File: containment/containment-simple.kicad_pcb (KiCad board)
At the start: 2 copper layers, 45.7 x 45.7 mm, 36 parts, among them J1 Conn_02x05_Odd_Even, J3 Conn_01x02, J4 Conn_01x02, J5 Conn_01x02, J6 Conn_01x02, Q1 BSS84, Q2 BSS84, Q3 BSS84, Q4 BSS84, U1 TMP411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

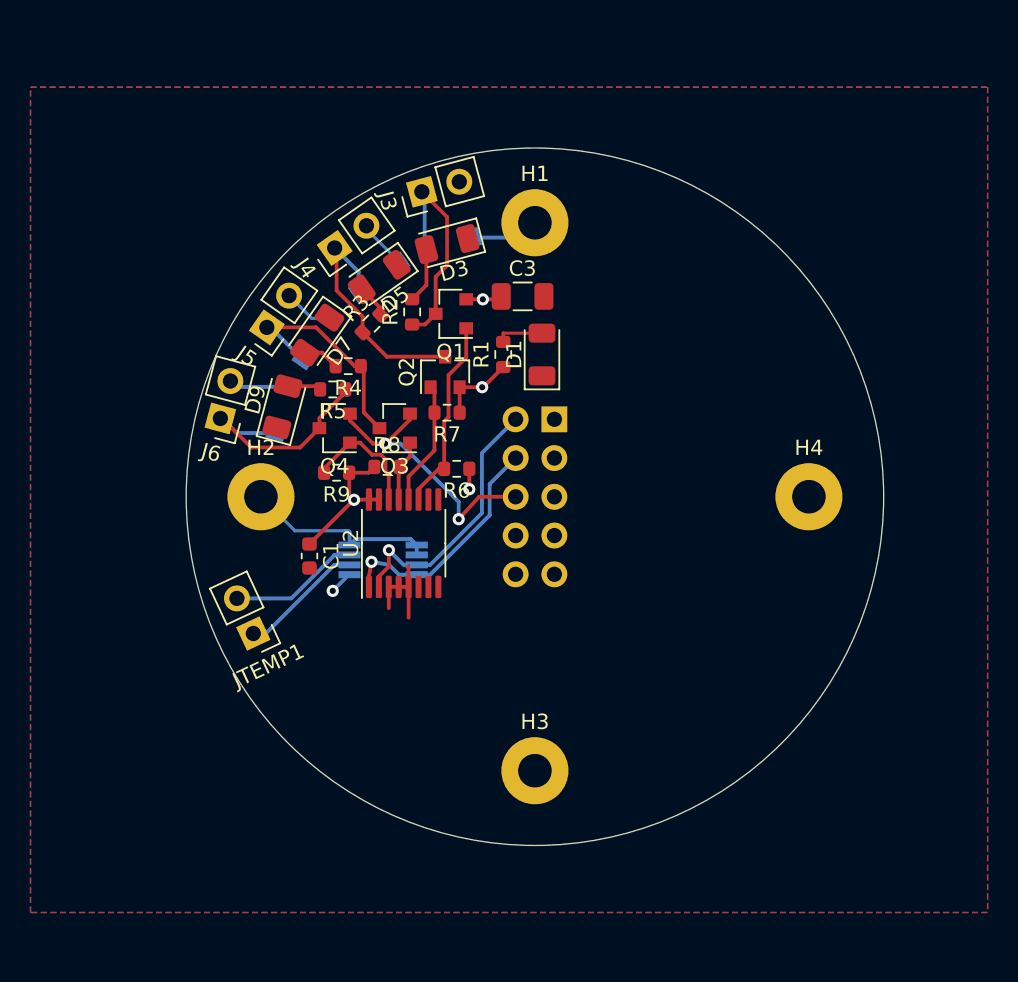
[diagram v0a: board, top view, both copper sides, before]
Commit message: add spixes
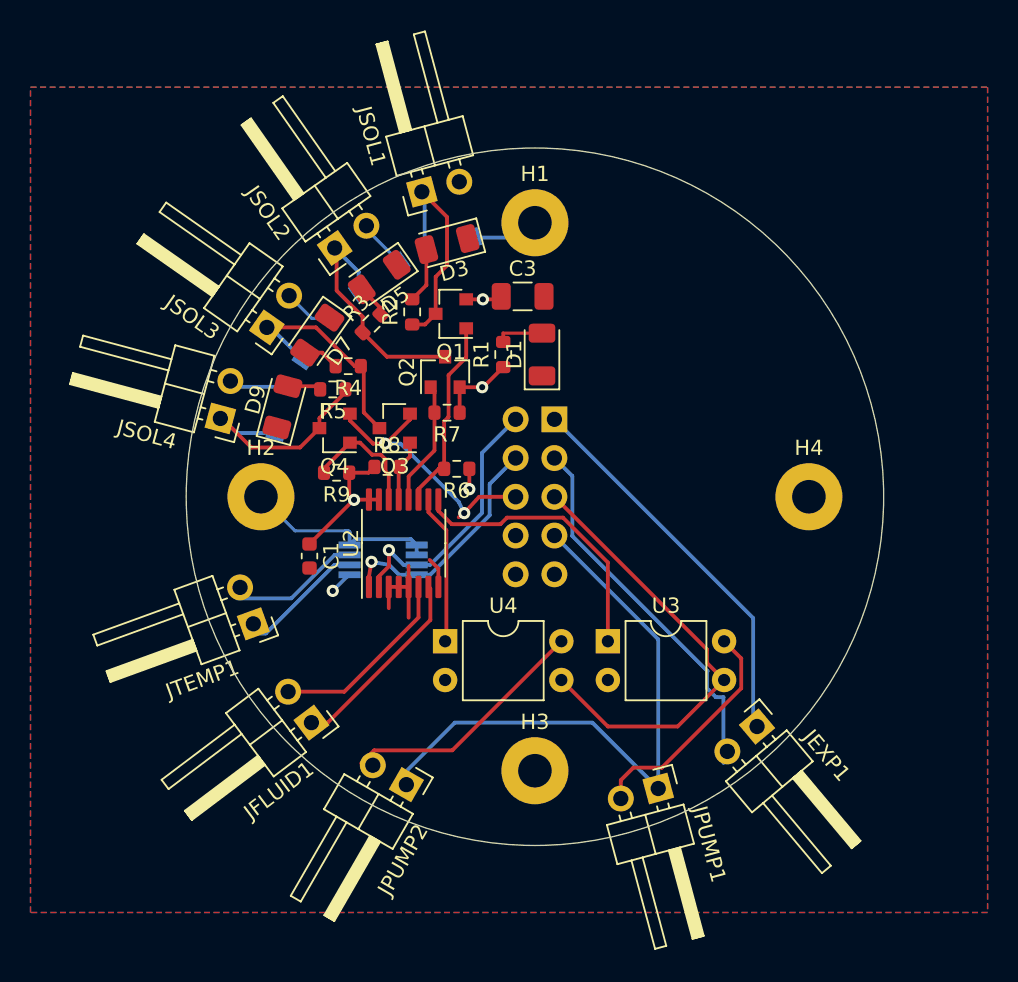
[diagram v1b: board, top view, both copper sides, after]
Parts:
- added JEXP1: Conn_01x02, Connector_PinHeader_2.54mm:PinHeader_1x02_P2.54mm_Horizontal, F.Cu at (154.6, 115.1)
- added JFLUID1: Conn_01x02, Connector_PinHeader_2.54mm:PinHeader_1x02_P2.54mm_Horizontal, F.Cu at (125.3, 114.8)
- added JPUMP1: Conn_01x02, Connector_PinHeader_2.54mm:PinHeader_1x02_P2.54mm_Horizontal, F.Cu at (148.1, 119.1)
- added JPUMP2: Conn_01x02, Connector_PinHeader_2.54mm:PinHeader_1x02_P2.54mm_Horizontal, F.Cu at (131.6, 118.9)
- added U3: SFH617A-1, Package_DIP:DIP-4_W7.62mm, F.Cu at (144.8, 109.5)
- added U4: SFH617A-1, Package_DIP:DIP-4_W7.62mm, F.Cu at (134.1, 109.5)
- JSOL1: renamed from J3; footprint Connector_PinHeader_2.54mm:PinHeader_1x02_P2.54mm_Vertical -> Connector_PinHeader_2.54mm:PinHeader_1x02_P2.54mm_Horizontal
- JSOL2: renamed from J4; footprint Connector_PinHeader_2.54mm:PinHeader_1x02_P2.54mm_Vertical -> Connector_PinHeader_2.54mm:PinHeader_1x02_P2.54mm_Horizontal
- JSOL3: renamed from J5; footprint Connector_PinHeader_2.54mm:PinHeader_1x02_P2.54mm_Vertical -> Connector_PinHeader_2.54mm:PinHeader_1x02_P2.54mm_Horizontal
- JSOL4: renamed from J6; footprint Connector_PinHeader_2.54mm:PinHeader_1x02_P2.54mm_Vertical -> Connector_PinHeader_2.54mm:PinHeader_1x02_P2.54mm_Horizontal
- JTEMP1: footprint Connector_PinHeader_2.54mm:PinHeader_1x02_P2.54mm_Vertical -> Connector_PinHeader_2.54mm:PinHeader_1x02_P2.54mm_Horizontal
- moved JTEMP1 0.63 mm to (121.5, 108.3), turned to 200 degrees
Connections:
- J1 pad 1: Net-(J1-Pad1) -> /experiment-
- J1 pad 3: Net-(J1-Pad3) -> /experiment+
- J1 pad 5: Net-(J1-Pad5) -> /HV-
- J1 pad 7: Net-(J1-Pad7) -> /HV+
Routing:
- net /HV+: track 0.00 -> 40.1 mm
- net /HV-: track 0.00 -> 29.8 mm
- net /experiment-: track 0.00 -> 26.3 mm
- net /experiment+: track 0.00 -> 24.9 mm
- net /p2: track 0.00 -> 18.8 mm
- net Net-(JPUMP2-Pad2): track 0.00 -> 16.4 mm
- net Net-(JPUMP1-Pad2): track 0.00 -> 15.1 mm
- net /p0: track 0.00 -> 12.9 mm
- net /p1: track 0.00 -> 12.8 mm
- net /p3: track 0.00 -> 9.81 mm
- net GND: track 33.5 -> 35.5 mm
- net +12V: track 18.1 -> 17.6 mm

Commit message: spikey 2
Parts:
- added JFLUID2: Conn_01x03, Connector_PinHeader_2.54mm:PinHeader_1x03_P2.54mm_Horizontal, F.Cu at (134.9, 120.3)
- JFLUID1: value Conn_01x02 -> Conn_01x03; footprint Connector_PinHeader_2.54mm:PinHeader_1x02_P2.54mm_Horizontal -> Connector_PinHeader_2.54mm:PinHeader_1x03_P2.54mm_Horizontal
- moved JPUMP2 16.4 mm to (148.0, 119.3), turned to 285 degrees
- moved JEXP1 7.51 mm to (158.4, 108.6), turned to 330 degrees
- moved JPUMP1 6.66 mm to (153.5, 115.3), turned to 310 degrees
- moved JFLUID1 1.71 mm to (126.6, 116.0), turned to 220 degrees
- moved U3 0.65 mm to (144.7, 108.8)
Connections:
- JFLUID1 pad 1: /p1 -> /p0
- JFLUID1 pad 2: /p0 -> +5V
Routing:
- net /HV+: track 40.1 -> 26.1 mm
- net Net-(JPUMP1-Pad2): track 15.1 -> 9.32 mm
- net /experiment+: track 24.9 -> 21.3 mm
- net /experiment-: track 26.3 -> 22.8 mm
- net Net-(JPUMP2-Pad2): track 16.4 -> 12.9 mm
- net /p1: track 12.8 -> 15.2 mm

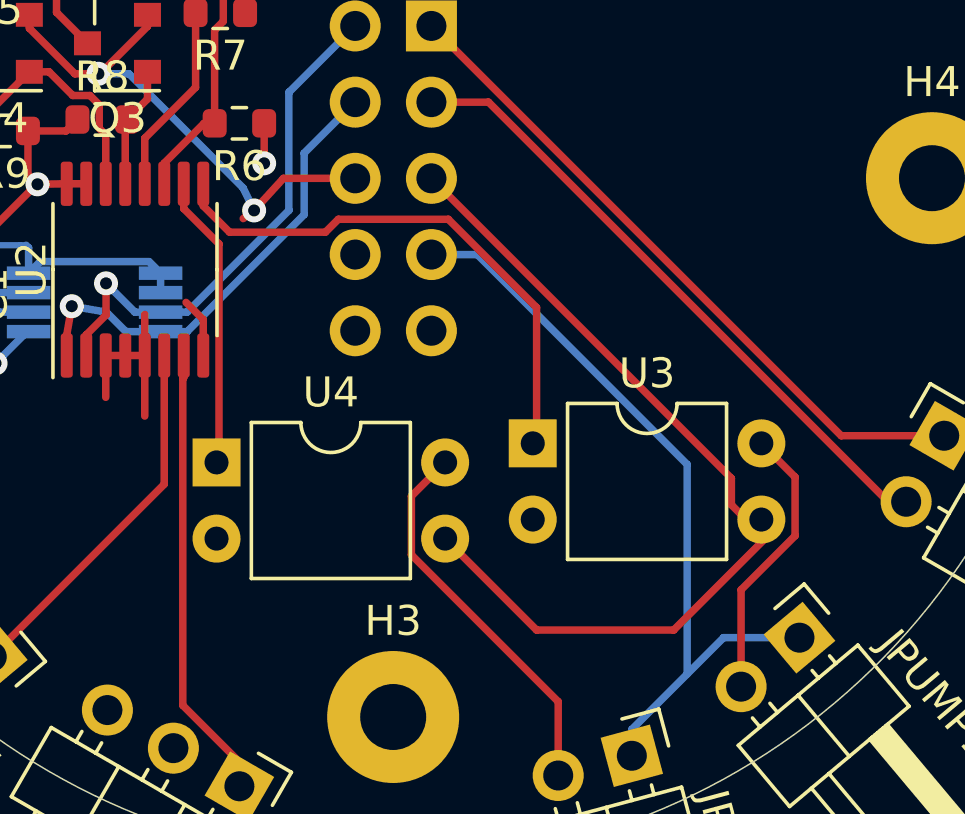
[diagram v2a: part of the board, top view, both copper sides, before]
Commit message: use the correct optocoupler
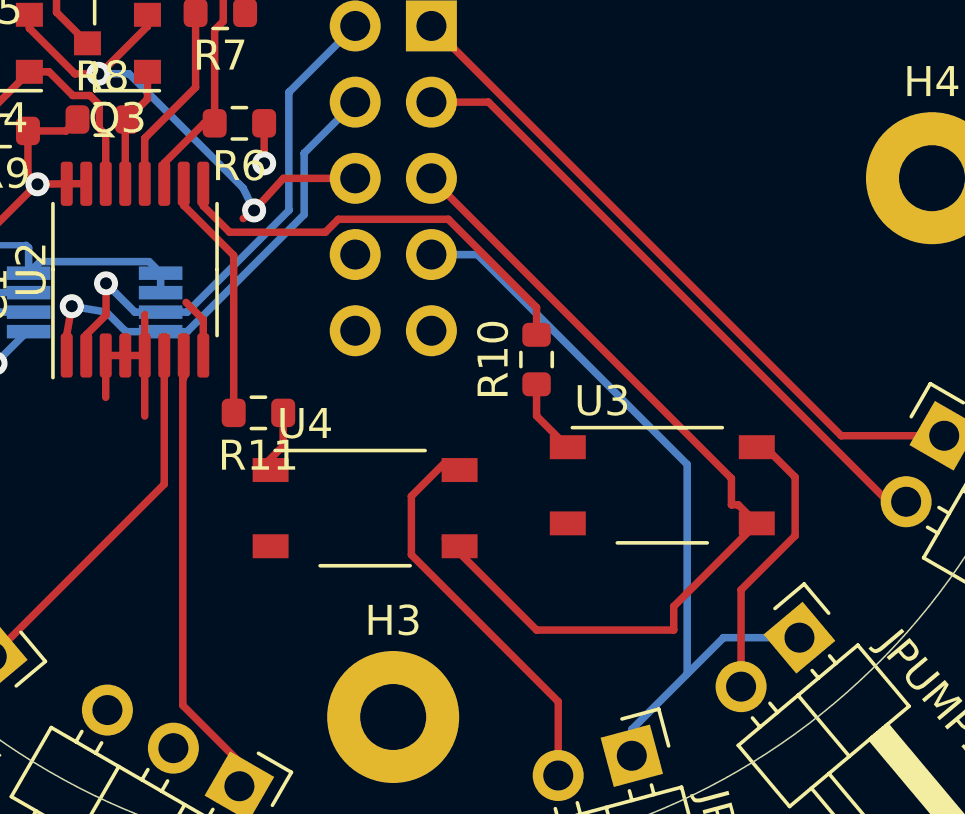
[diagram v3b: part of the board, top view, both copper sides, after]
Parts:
- added R10: 470, Resistor_SMD:R_0603_1608Metric, F.Cu at (144.8, 106.0)
- added R11: 470, Resistor_SMD:R_0603_1608Metric, F.Cu at (135.5, 107.8)
- U3, U4: value SFH617A-1 -> TLP175A; footprint Package_DIP:DIP-4_W7.62mm -> Package_SO:MFSOP6-4_4.4x3.6mm_P1.27mm
- moved U4 5.18 mm to (139.1, 111.0)
- moved U3 4.54 mm to (149.0, 110.2)
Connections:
- U3 pad 1: /p2 -> Net-(R10-Pad1)
- U3 pad 3: /HV- -> GND
- U3 pad 4: Net-(JPUMP1-Pad2) -> /HV-
- U4 pad 1: /p3 -> Net-(R11-Pad1)
- U4 pad 3: /HV- -> GND
- U4 pad 4: Net-(JPUMP2-Pad2) -> /HV-
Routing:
- net /p2: track 18.8 -> 14.5 mm
- net Net-(R10-Pad1): track 0.00 -> 2.53 mm
- net Net-(R11-Pad1): track 0.00 -> 1.88 mm
- net /p3: track 9.81 -> 8.33 mm

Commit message: inner containment baord lookin pretty good
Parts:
- removed D2: D, Diode_SMD:D_SOD-123
- removed D3: LED, LED_SMD:LED_1206_3216Metric
- removed JFLUID1, JFLUID2: Conn_01x03, Connector_PinHeader_2.54mm:PinHeader_1x03_P2.54mm_Horizontal
- removed JSOL1: Conn_01x02, Connector_PinHeader_2.54mm:PinHeader_1x02_P2.54mm_Horizontal
- removed R2: 1k, Resistor_SMD:R_0603_1608Metric
- removed R6: 10k, Resistor_SMD:R_0603_1608Metric
- added C2: .1uF, Capacitor_SMD:C_0603_1608Metric, F.Cu at (137.8, 111.8)
- added C4: .1uF, Capacitor_SMD:C_0603_1608Metric, F.Cu at (144.7, 107.1)
- added C5: .1uF, Capacitor_SMD:C_0603_1608Metric, F.Cu at (126.6, 111.8)
- added J2: Conn_01x03, Connector_JST:JST_PH_S3B-PH-K_1x03_P2.00mm_Horizontal, F.Cu at (153.9, 109.6)
- added J3: Conn_01x03, Connector_JST:JST_PH_S3B-PH-K_1x03_P2.00mm_Horizontal, F.Cu at (149.0, 114.0)
- added Q5: BC846, Package_TO_SOT_SMD:SOT-23, F.Cu at (135.3, 120.1)
- added Q6: BC846, Package_TO_SOT_SMD:SOT-23, F.Cu at (144.7, 115.4)
- added R12: 10k, Resistor_SMD:R_0603_1608Metric, F.Cu at (148.8, 104.2)
- added R13: 50, Resistor_SMD:R_0603_1608Metric, F.Cu at (131.1, 119.4)
- added R14: 10k, Resistor_SMD:R_0603_1608Metric, F.Cu at (148.8, 106.2)
- added R15: 10k, Resistor_SMD:R_0603_1608Metric, F.Cu at (151.1, 110.6)
- added R16: 10k, Resistor_SMD:R_0603_1608Metric, F.Cu at (149.5, 108.3)
- added R18: 50, Resistor_SMD:R_0603_1608Metric, F.Cu at (144.1, 118.8)
- added R20: 10k, Resistor_SMD:R_0603_1608Metric, F.Cu at (149.5, 110.6)
- added U5: LM358, Package_SO:SOIC-8_3.9x4.9mm_P1.27mm, F.Cu at (133.2, 115.5)
- added U6: LM339, Package_SO:TSSOP-14_4.4x5mm_P0.65mm, F.Cu at (142.7, 110.8)
- added U7: MCP4725xxx-xCH, Package_TO_SOT_SMD:SOT-23-6, F.Cu at (131.4, 110.3)
- added U8: MCP4725xxx-xCH, Package_TO_SOT_SMD:SOT-23-6, F.Cu at (135.2, 110.3)
- D1, D5, D7, D9: footprint LED_SMD:LED_1206_3216Metric -> LED_SMD:LED_0603_1608Metric
- D4, D6, D8: footprint Diode_SMD:D_SOD-123 -> Diode_SMD:D_SOD-323F; moved to F.Cu
- JEXP1, JPUMP1, JPUMP2, JSOL2, JSOL3, JSOL4, JTEMP1: footprint Connector_PinHeader_2.54mm:PinHeader_1x02_P2.54mm_Horizontal -> Connector_JST:JST_PH_S2B-PH-K_1x02_P2.00mm_Horizontal
- U1: moved to F.Cu
- moved JPUMP1 28.2 mm to (152.3, 87.2), turned to 90 degrees
- moved JEXP1 27.8 mm to (147.6, 82.9), turned to 180 degrees
- moved JPUMP2 25.6 mm to (153.4, 94.2), turned to 90 degrees
- moved U4 23.5 mm to (147.3, 89.0), turned to 90 degrees
- moved U3 22.1 mm to (143.1, 89.0), turned to 90 degrees
- moved R11 17.7 mm to (147.6, 94.9), turned to 270 degrees
- moved Q1 13.6 mm to (144.9, 96.8)
- moved R10 11.9 mm to (145.2, 94.1), turned to 180 degrees
- moved C3 11.3 mm to (135.4, 97.5), turned to 270 degrees
- moved U1 11.2 mm to (125.5, 114.4), turned to 315 degrees
- moved D5 9.66 mm to (138.5, 89.8), turned to 90 degrees
- moved R3 7.71 mm to (136.9, 89.8), turned to 90 degrees
- moved JSOL2 7.59 mm to (134.4, 84.9), turned to 180 degrees
- moved JSOL3 6.60 mm to (128.0, 85.3), turned to 270 degrees
- moved D7 6.36 mm to (131.4, 92.2), turned to 270 degrees
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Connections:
- J1 pad 1: /experiment- -> GND
- J1 pad 3: /experiment+ -> /experiment
- J1 pad 7: /HV+ -> GND
- J1 pad 9: Net-(J1-Pad9) -> /HV+
- JEXP1 pad 1: /experiment- -> /experiment
- JEXP1 pad 2: /experiment+ -> GND
- JSOL2 pad 1: Net-(D4-Pad1) -> GND
- JSOL2 pad 2: GND -> Net-(D4-Pad1)
- JSOL3 pad 1: Net-(D6-Pad1) -> GND
- JSOL3 pad 2: GND -> Net-(D6-Pad1)
- JSOL4 pad 1: Net-(D8-Pad1) -> GND
- JSOL4 pad 2: GND -> Net-(D8-Pad1)
- Q1 pad 2: +5V -> Net-(Q1-Pad2)
- Q1 pad 3: Net-(D2-Pad1) -> +5V
- R10 pad 2: /p2 -> Net-(Q1-Pad2)
- R11 pad 2: /p3 -> /p4
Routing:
- net GND: track 35.5 -> 66.9 mm, vias 0 -> 2
- net Net-(J2-Pad2): track 0.00 -> 30.3 mm, vias 0 -> 1
- net +5V: track 19.8 -> 50.0 mm, vias 5 -> 9
- net Net-(J3-Pad1): track 0.00 -> 26.8 mm
- net /experiment-: track 22.8 -> 0.00 mm
- net scl: track 15.8 -> 38.3 mm, vias 1 -> 2
- net /experiment+: track 21.3 -> 0.00 mm
- net sda: track 17.6 -> 38.1 mm
- net Net-(J2-Pad1): track 0.00 -> 19.3 mm, vias 0 -> 1
- net /experiment: track 0.00 -> 17.2 mm
- net /Fluid Sensors/2_3rds: track 0.00 -> 14.9 mm
- net Net-(D2-Pad1): track 14.8 -> 0.00 mm
- net /Fluid Sensors/1_3rds: track 0.00 -> 13.5 mm
- net Net-(Q6-Pad2): track 0.00 -> 11.1 mm
- net /p3: track 8.33 -> 19.3 mm
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
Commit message: can i get a go dawgs
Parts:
- added C6: .1uF, Capacitor_SMD:C_0603_1608Metric, F.Cu at (149.4, 110.6)
- added R17: 10k, Resistor_SMD:R_0603_1608Metric, F.Cu at (136.4, 103.3)
- added R19: 10k, Resistor_SMD:R_0603_1608Metric, F.Cu at (144.7, 105.6)
- added R2: 10k, Resistor_SMD:R_0603_1608Metric, F.Cu at (134.9, 106.4)
- added R6: 10k, Resistor_SMD:R_0603_1608Metric, F.Cu at (137.9, 108.6)
- moved R15 4.64 mm to (151.3, 106.0)
- moved R20 1.53 mm to (151.0, 110.6), turned to 270 degrees
- renumbered J2 to JFLUID1, J3 to JFLUID2
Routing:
- net +5V: track 50.0 -> 58.0 mm, vias 9 -> 10
- net /p3: track 19.3 -> 23.0 mm
- net GND: track 66.9 -> 65.1 mm, vias 2 -> 1
- net /Fluid Sensors/1_3rds: track 13.5 -> 14.9 mm
- net Net-(JFLUID2-Pad1): track 26.8 -> 27.9 mm
- net /p2: track 17.1 -> 18.2 mm
- net /p1: track 8.43 -> 9.05 mm
- net /p0: track 9.35 -> 9.88 mm

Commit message: ordered it supposedly
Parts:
- renumbered JSOL2 to JSOL1, JSOL3 to JSOL2, JSOL4 to JSOL3
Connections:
- Q1 pad 2: Net-(Q1-Pad2) -> +5V
- Q1 pad 3: +5V -> Net-(Q1-Pad3)
- Q2 pad 2: +5V -> +12V
- R10 pad 2: Net-(Q1-Pad2) -> Net-(Q1-Pad3)
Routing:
- net +12V: track 19.1 -> 24.7 mm
- net GND: track 65.1 -> 68.8 mm
- net Net-(Q1-Pad3): track 0.00 -> 2.84 mm
- net Net-(Q1-Pad2): track 2.37 -> 0.00 mm
- net /p4: track 22.2 -> 23.2 mm
- net +5V: track 58.0 -> 57.0 mm
- net /HV+: track 25.0 -> 25.7 mm

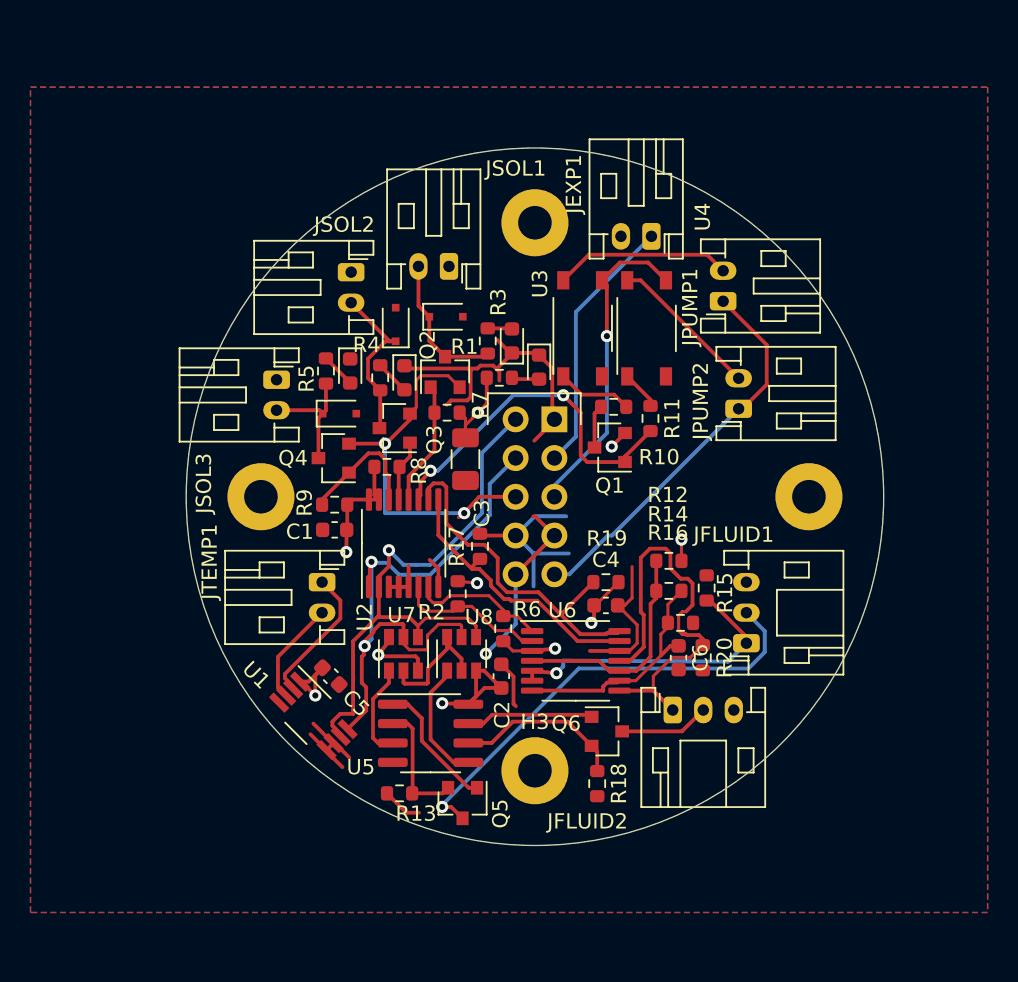
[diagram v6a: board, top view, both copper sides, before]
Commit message: containment schematic updated to include experiment & correct voltage on valve mosfets
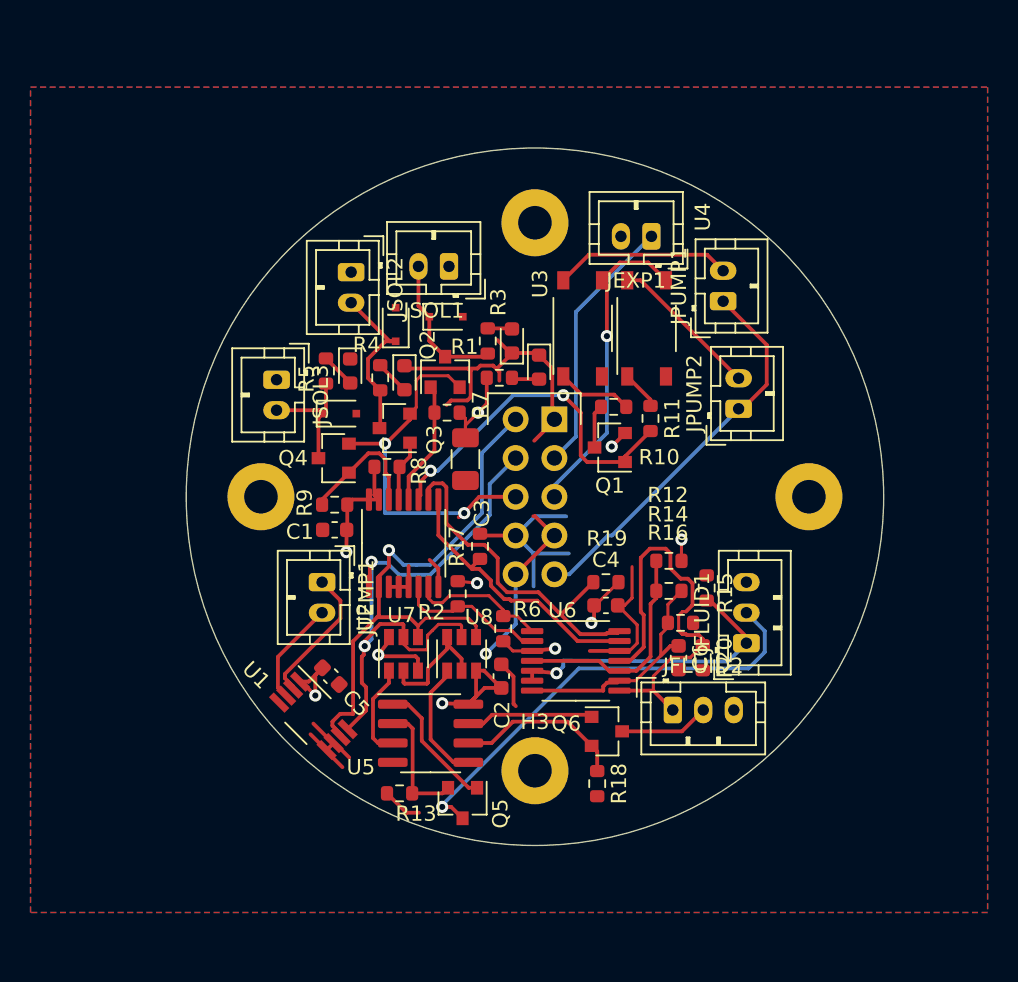
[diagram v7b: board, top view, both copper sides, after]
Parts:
- JEXP1, JPUMP1, JPUMP2, JSOL1, JSOL2, JSOL3, JTEMP1: footprint Connector_JST:JST_PH_S2B-PH-K_1x02_P2.00mm_Horizontal -> Connector_JST:JST_PH_B2B-PH-K_1x02_P2.00mm_Vertical
- JFLUID1, JFLUID2: footprint Connector_JST:JST_PH_S3B-PH-K_1x03_P2.00mm_Horizontal -> Connector_JST:JST_PH_B3B-PH-K_1x03_P2.00mm_Vertical
